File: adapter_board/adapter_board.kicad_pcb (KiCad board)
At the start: 2 copper layers, 92 x 86.3 mm, 19 parts, among them J1 Conn_01x05_Female, J10 Conn_01x04_Female, J11 Conn_01x04_Female, J12 Conn_01x04_Female, J13 Conn_01x04_Female, J14 Conn_01x04_Female, J2 Conn_01x12_Female, J3 Conn_01x04_Female, J4 Conn_01x02_Female, J5 Conn_01x05_Female, J6 Conn_01x04_Female, J7 Conn_01x06_Female, J8 Conn_01x06_Female, J9 Conn_01x04_Female, U1 PC104

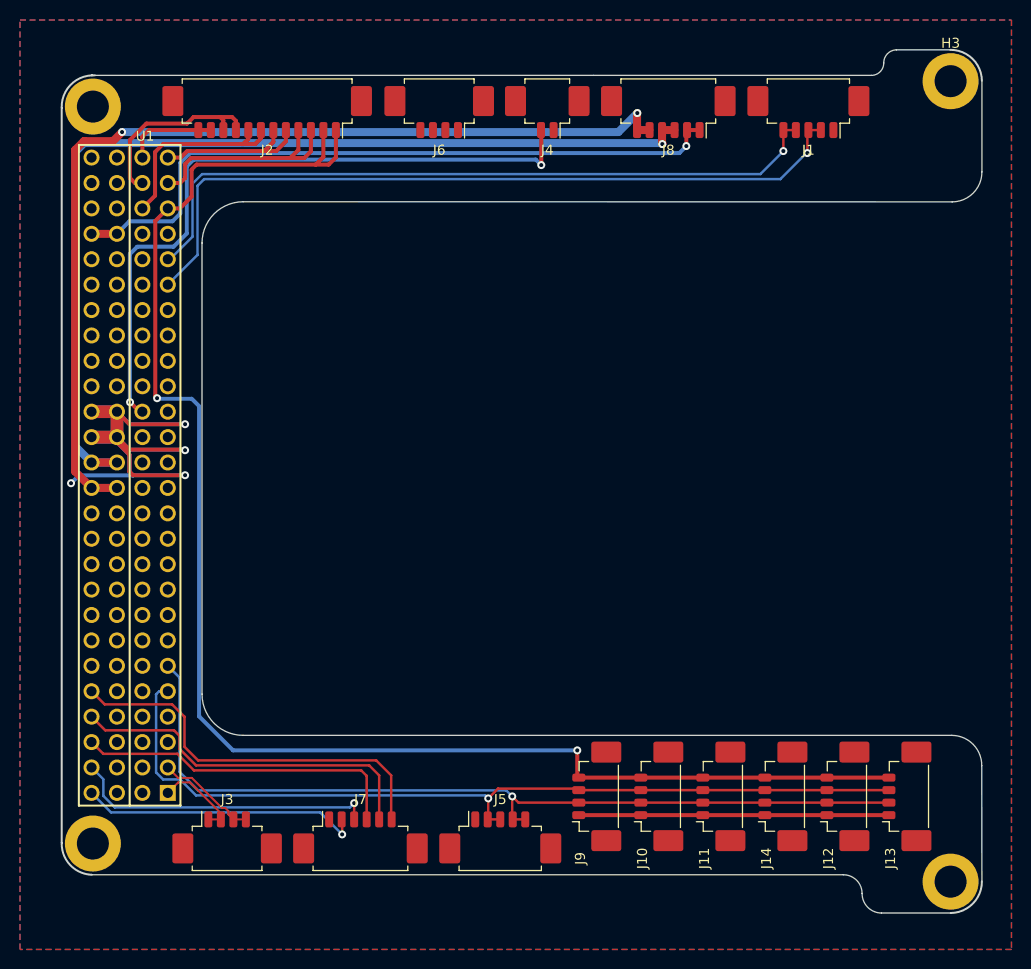
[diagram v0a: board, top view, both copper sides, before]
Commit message: added labels to and generated gerber for adapter board
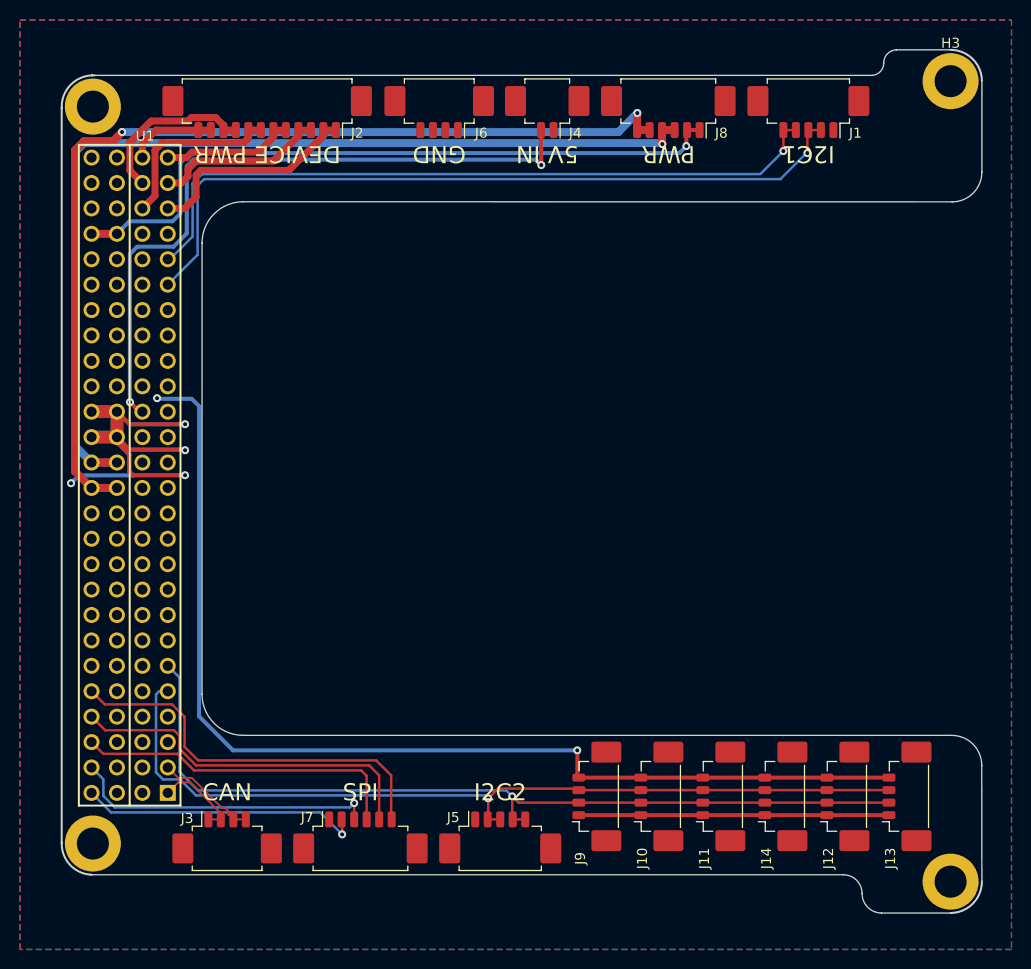
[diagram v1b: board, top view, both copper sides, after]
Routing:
- net /OUT1: track 155.1 -> 130.2 mm
- net /OUT2: track 21.9 -> 17.2 mm
- net /OUT3: track 16.3 -> 13.3 mm
- net /OUT5: track 19.3 -> 17.0 mm
- net /OUT4: track 19.9 -> 18.2 mm
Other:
- board text added: "5V IN"
- board text added: "CAN"
- board text added: "DEVICE PWR"
- board text added: "GND"
- board text added: "I2C1"
- board text added: "I2C2"
- board text added: "PWR"
- board text added: "SPI"

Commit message: changed silkscreen labels for adapter board
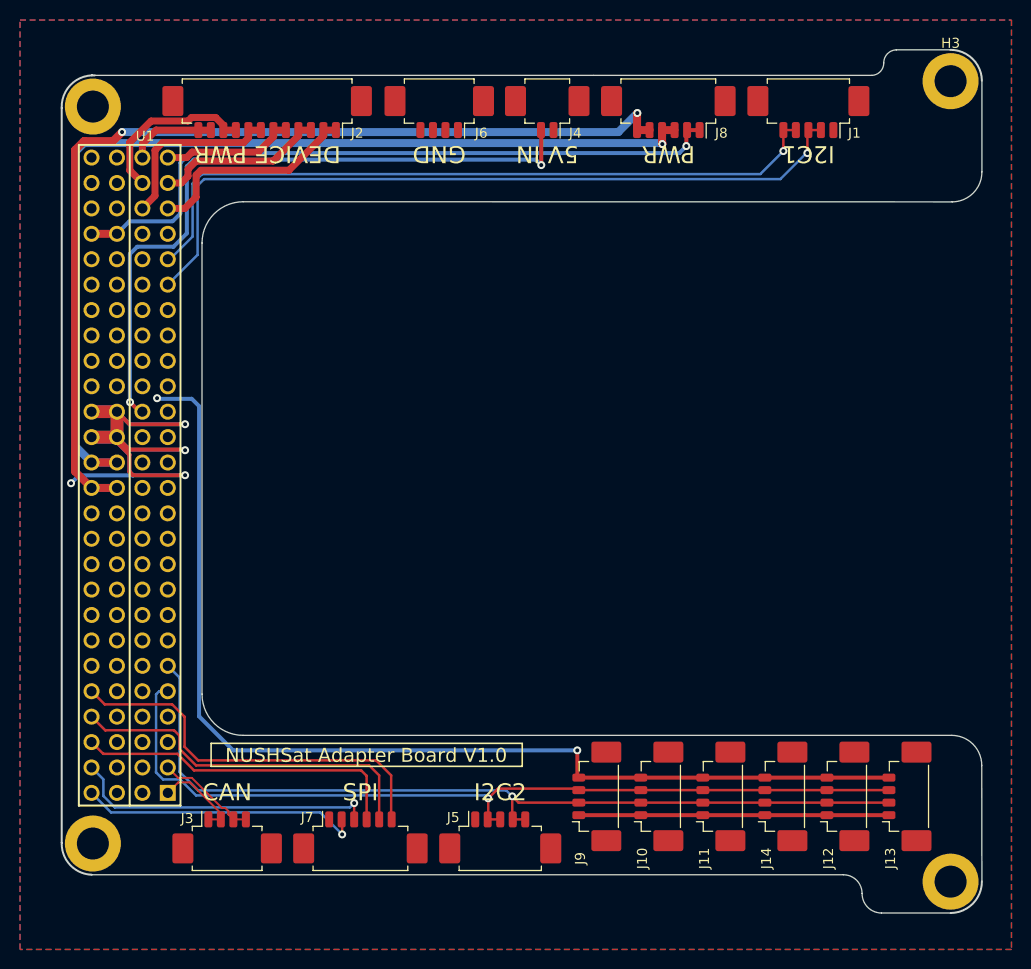
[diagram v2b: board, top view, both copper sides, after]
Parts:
- added G***: LOGO, cubesat_obc:nush, B.Cu at (188.1, 124.9)
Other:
- board text added: "Lin Yicheng"
- board text added: "NUSHSat Adapter Board V1.0"
